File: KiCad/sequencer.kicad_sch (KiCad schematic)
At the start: 36 parts, among them J1 CLOCK OUT, J2 GATE OUT, J3 CLOCK IN, J4 CV OUT, J5 RESET, Q1 BC848W, SW1 SW_Nidec_CAS-120A1, U1 TL074

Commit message: adding footprints
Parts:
- RV1, RV2: footprint (none) -> Eurorack:3296W1503LF
- SW1: footprint Button_Switch_SMD:Nidec_Copal_CAS-120A -> Eurorack:2MS1T1B1M2QES
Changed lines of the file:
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@@
 			)
 		)
-		(property "Footprint" ""
+		(property "Footprint" "Eurorack:3296W1503LF"
 			(at 215.9 149.86 0)
 			(effects
@@
 			)
 		)
-		(property "Footprint" "Button_Switch_SMD:Nidec_Copal_CAS-120A"
+		(property "Footprint" "Eurorack:2MS1T1B1M2QES"
 			(at 203.2 142.24 0)
 			(effects
@@
 			)
 		)
-		(property "Footprint" ""
+		(property "Footprint" "Eurorack:3296W1503LF"
 			(at 229.87 149.86 0)
 			(effects

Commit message: initiating pcb layout
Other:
- note added: "RV1 and RV2 are Trimmer Potentiometer"
- moved on the sheet: TP3
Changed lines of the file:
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@@
 		(title "8 Step Sequencer")
 		(date "2026-03-13")
-		(rev "v0.0")
+		(rev "v1.0")
 		(company "Dirty Dream - Nathanael Noir")
 	)
@@
 		)
 	)
+	(text "RV1 and RV2 \nare \nTrimmer Potentiometer"
+		(exclude_from_sim no)
+		(at 248.666 157.734 0)
+		(effects
+			(font
+				(size 1.27 1.27)
+			)
+		)
+	)
 	(text "TEST POINTS GND\n"
 		(exclude_from_sim no)
@@
 	)
 	(junction
-		(at 67.31 130.81)
+		(at 74.93 130.81)
 		(diameter 0)
 		(color 0 0 0 0)
@@
 	(wire
 		(pts
+			(xy 74.93 130.81) (xy 116.84 130.81)
+		)
+		(stroke
+			(width 0)
+			(type default)
+		)
+	)
+	(wire
+		(pts
 			(xy 229.87 144.78) (xy 229.87 146.05)
 		)
@@
 	(wire
 		(pts
-			(xy 116.84 130.81) (xy 67.31 130.81)
-		)
-		(stroke
-			(width 0)
-			(type default)
-		)
-	)
-	(wire
-		(pts
 			(xy 259.08 33.02) (xy 259.08 38.1)
 		)
@@
 	(wire
 		(pts
-			(xy 62.23 130.81) (xy 67.31 130.81)
+			(xy 62.23 130.81) (xy 74.93 130.81)
 		)
 		(stroke
@@
 	(symbol
 		(lib_id "Connector:TestPoint")
-		(at 67.31 130.81 0)
+		(at 74.93 130.81 0)
 		(unit 1)
 		(exclude_from_sim no)
@@
 		(dnp no)
 		(property "Reference" "TP3"
-			(at 65.532 121.412 0)
+			(at 73.152 121.412 0)
 			(effects
 				(font
@@
 		)
 		(property "Value" "C"
-			(at 66.548 124.4601 0)
+			(at 74.168 124.4601 0)
 			(effects
 				(font
@@
 		)
 		(property "Footprint" "TestPoint:TestPoint_Pad_D1.5mm"
-			(at 72.39 130.81 0)
+			(at 80.01 130.81 0)
 			(effects
 				(font
@@
 		)
 		(property "Datasheet" "~"
-			(at 72.39 130.81 0)
+			(at 80.01 130.81 0)
 			(effects
 				(font
@@
 		)
 		(property "Description" "test point"
-			(at 67.31 130.81 0)
+			(at 74.93 130.81 0)
 			(effects
 				(font
@@
 		)
 		(property "Availability" ""
-			(at 67.31 130.81 0)
+			(at 74.93 130.81 0)
 			(effects
 				(font
@@
 		)
 		(property "Check_prices" ""
-			(at 67.31 130.81 0)
+			(at 74.93 130.81 0)
 			(effects
 				(font
@@
 		)
 		(property "Description_1" ""
-			(at 67.31 130.81 0)
+			(at 74.93 130.81 0)
 			(effects
 				(font
@@
 		)
 		(property "MANUFACTURER" ""
-			(at 67.31 130.81 0)
+			(at 74.93 130.81 0)
 			(effects
 				(font
@@
 		)
 		(property "MAXIMUM_PACKAGE_HEIGHT" ""
-			(at 67.31 130.81 0)
+			(at 74.93 130.81 0)
 			(effects
 				(font
@@
 		)
 		(property "MF" ""
-			(at 67.31 130.81 0)
+			(at 74.93 130.81 0)
 			(effects
 				(font
@@
 		)
 		(property "MP" ""
-			(at 67.31 130.81 0)
+			(at 74.93 130.81 0)
 			(effects
 				(font
@@
 		)
 		(property "PARTREV" ""
-			(at 67.31 130.81 0)
+			(at 74.93 130.81 0)
 			(effects
 				(font
@@
 		)
 		(property "Package" ""
-			(at 67.31 130.81 0)
+			(at 74.93 130.81 0)
 			(effects
 				(font
@@
 		)
 		(property "Price" ""
-			(at 67.31 130.81 0)
+			(at 74.93 130.81 0)
 			(effects
 				(font
@@
 		)
 		(property "STANDARD" ""
-			(at 67.31 130.81 0)
+			(at 74.93 130.81 0)
 			(effects
 				(font
@@
 		)
 		(property "SnapEDA_Link" ""
-			(at 67.31 130.81 0)
-			(effects
-				(font
+			(at 74.93 130.81 0)
+			(effects
+				(font

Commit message: placing layout frontview
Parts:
- R13: value 51k -> 18k
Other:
- note added: "Adjust to get 2.5V max. output"
- note added: "Adjust to get 5V max. output"

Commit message: re-placing components; optimizing text on silkscreen
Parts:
- RV1, RV2: footprint Eurorack:3296W1503LF -> Eurorack:Trimmer_Bourns_3296W_50k_THT
- SW1: footprint Eurorack:2MS1T1B1M2QES -> Eurorack:Switch_Toggle_Dailywell_MS1T1B1M2QES_SPDT
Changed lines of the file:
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@@
 			)
 		)
-		(property "Footprint" "Eurorack:3296W1503LF"
+		(property "Footprint" "Eurorack:Trimmer_Bourns_3296W_50k_THT"
 			(at 215.9 149.86 0)
 			(effects
@@
 			)
 		)
-		(property "Footprint" "Eurorack:2MS1T1B1M2QES"
+		(property "Footprint" "Eurorack:Switch_Toggle_Dailywell_MS1T1B1M2QES_SPDT"
 			(at 203.2 142.24 0)
 			(effects
@@
 			)
 		)
-		(property "Footprint" "Eurorack:3296W1503LF"
+		(property "Footprint" "Eurorack:Trimmer_Bourns_3296W_50k_THT"
 			(at 229.87 149.86 0)
 			(effects

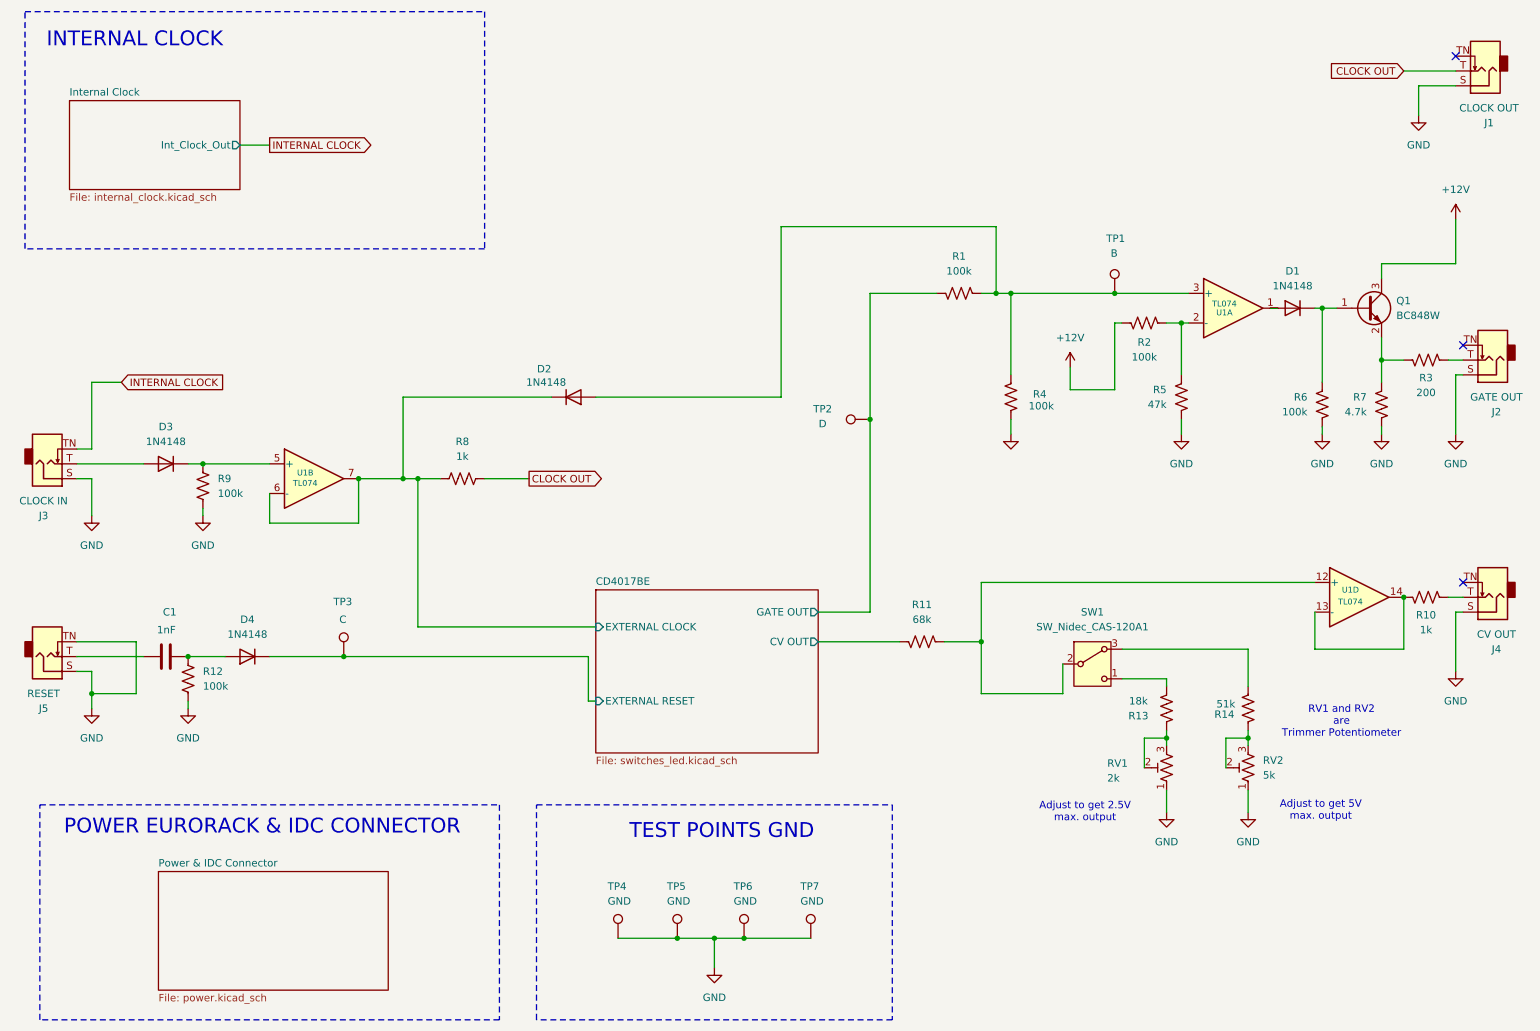
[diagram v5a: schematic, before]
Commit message: changing position on silkscreen
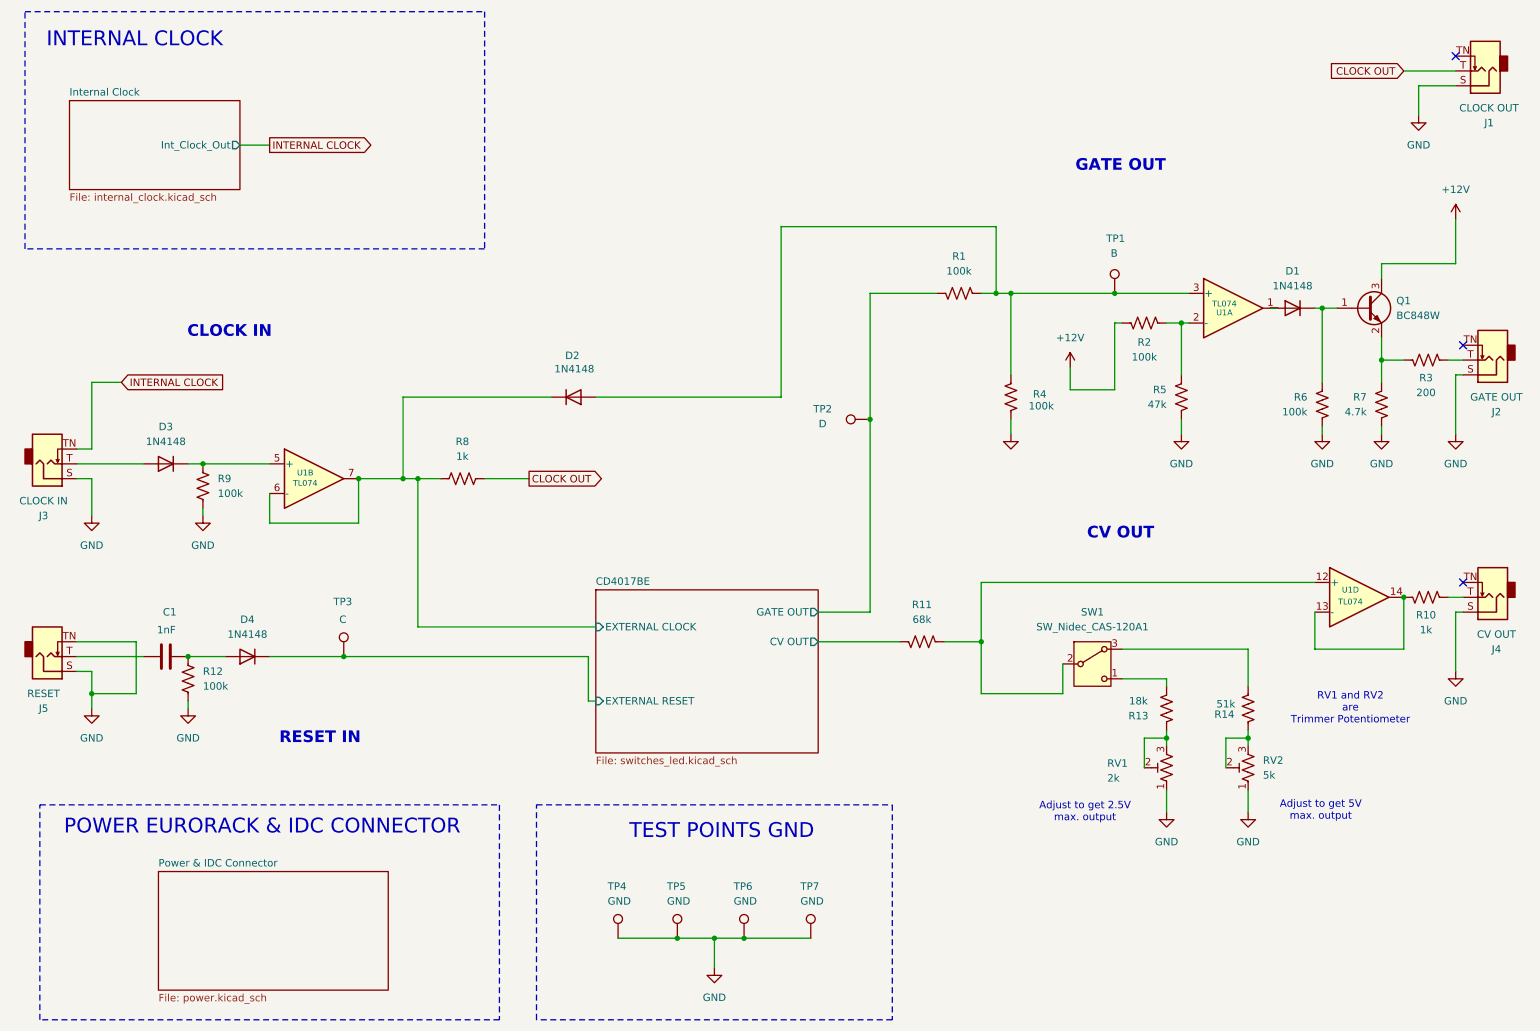
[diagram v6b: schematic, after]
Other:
- note added: "CLOCK IN"
- note added: "CV OUT"
- note added: "GATE OUT"
- note added: "RESET IN"
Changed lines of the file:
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@@
 	(text "RV1 and RV2 \nare \nTrimmer Potentiometer"
 		(exclude_from_sim no)
-		(at 245.872 141.986 0)
+		(at 247.396 139.7 0)
 		(effects
 			(font
@@
 		)
 	)
+	(text "CV OUT"
+		(exclude_from_sim no)
+		(at 208.026 109.728 0)
+		(effects
+			(font
+				(size 2 2)
+				(thickness 0.254)
+				(bold yes)
+			)
+		)
+	)
+	(text "GATE OUT"
+		(exclude_from_sim no)
+		(at 208.026 46.736 0)
+		(effects
+			(font
+				(size 2 2)
+				(thickness 0.254)
+				(bold yes)
+			)
+		)
+	)
+	(text "RESET IN\n"
+		(exclude_from_sim no)
+		(at 70.866 144.78 0)
+		(effects
+			(font
+				(size 2 2)
+				(thickness 0.254)
+				(bold yes)
+			)
+		)
+	)
+	(text "CLOCK IN"
+		(exclude_from_sim no)
+		(at 55.372 75.184 0)
+		(effects
+			(font
+				(size 2 2)
+				(thickness 0.254)
+				(bold yes)
+			)
+		)
+	)
 	(junction
 		(at 215.9 144.78)
@@
 		(dnp no)
 		(property "Reference" "D2"
-			(at 110.49 81.534 0)
+			(at 115.316 79.248 0)
 			(effects
 				(font
@@
 		)
 		(property "Value" "1N4148"
-			(at 113.0301 83.82 0)
+			(at 117.8561 81.534 0)
 			(effects
 				(font

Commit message: new logo, via correction, gerber
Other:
- company: Dirty Dream - Nathanael Noir -> © Dirty Dream - Nathanael Noir
- title: 8 Step Sequencer -> Modulo-8 Seqencer
